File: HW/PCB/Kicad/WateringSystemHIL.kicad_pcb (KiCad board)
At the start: 4 copper layers, 100 x 100 mm, 50 parts, among them J1 USB_B_Micro_VBUS_Input, J13 USB_B_Micro, J16 Boot_H, J17 Boot_L, J18 Encoder_PINA, J19 Encoder_PINB, J20 Encoder_SW, J3 Raspberry Pi Zero WH, J4 MEAS_VIN, J5 MEAS_I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

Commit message: PCB v0.9.1
Added
- Status LEDs for Power, DUT Power, Linked

Changed
- Active signal state of DUT->TS LED and TS->DUT LED. Turn ON the LEDs when the signals are Low level.

Fixed
- An issue where the micro USB plug could not be mounted on the PCB properlly. The micro USB plub was replaced with GCT USB3150.
- An issue where boot mode of WateringSystem was not properlly controlled. Use 74HC244 to control Boot_L signal.
- An issue where power switch of WateringSystem was not properlly controlled. Use a P-Channel MOSFET(AO3401) instead of N-Channel MOSFET(AO3400).
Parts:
- removed J13: USB_B_Micro, WateringSystemHIL:BKL_MicroUSBPlug_10120262
- removed J16: Boot_H, WateringSystemHIL:P100-E2 Pogo Spring Test Probe Pin
- removed Q3: AO3400A, Package_TO_SOT_SMD:SOT-23
- removed R16, R21: 10k, Capacitor_SMD:C_0805_2012Metric_Pad1.18x1.45mm_HandSolder
- added D5: LED_Small, LED_SMD:LED_0603_1608Metric_Pad1.05x0.95mm_HandSolder, F.Cu at (188.4, 131.7)
- added D6: LED_Small, LED_SMD:LED_0603_1608Metric_Pad1.05x0.95mm_HandSolder, F.Cu at (188.4, 133.9)
- added J2: USB_B_Micro, WateringSystemHIL:GCT_USB3150-30-130-A, F.Cu at (149.6, 59.2)
- added R13: 10k, Capacitor_SMD:C_0805_2012Metric_Pad1.18x1.45mm_HandSolder, F.Cu at (184.0, 131.7)
- added R14: 10k, Capacitor_SMD:C_0805_2012Metric_Pad1.18x1.45mm_HandSolder, F.Cu at (184.0, 133.9)
- Q1: value AO3400A -> AO3401A; footprint Package_TO_SOT_SMD:SOT-23 -> Package_TO_SOT_SMD:SOT-23_Handsoldering
- R6: value 10k -> 100
- R8: value 10k -> 10m
- moved R7 7.76 mm to (133.0, 56.2)
- moved R12 3.52 mm to (121.7, 134.6)
- moved D3 2.80 mm to (188.3, 136.2)
- moved R9 2.80 mm to (184.0, 136.2)
- moved D2 1.60 mm to (188.4, 138.4), turned to 180 degrees
- moved R5 1.60 mm to (184.0, 138.4), turned to 0 degrees
- moved D4 0.91 mm to (188.5, 142.8)
- moved R23 0.91 mm to (184.0, 142.8)
- moved Q1 0.82 mm to (133.0, 60.7), turned to 270 degrees
- moved R4 0.30 mm to (184.0, 140.6), turned to 0 degrees
- moved D1 0.28 mm to (188.4, 140.6), turned to 180 degrees
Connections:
- J3 pad 10: Net-(D2-Pad2) -> Net-(D2-Pad1)
- J3 pad 12: CTL_BOOT -> Net-(J3-Pad12)
- J3 pad 40: Net-(J3-Pad40) -> CTL_BOOT
- J3 pad 8: Net-(D1-Pad2) -> Net-(D1-Pad1)
- J7 pad 1: Net-(D1-Pad2) -> Net-(D1-Pad1)
- J8 pad 1: Net-(D2-Pad2) -> Net-(D2-Pad1)
- Q1 pad 2: Net-(Q1-Pad2) -> +5V
- Q1 pad 3: +5V -> Net-(Q1-Pad3)
- R10 pad 2: Net-(Q1-Pad2) -> Net-(Q1-Pad3)
- R4 pad 1: Net-(D1-Pad1) -> +3V3
- R4 pad 2: GND -> Net-(D1-Pad2)
- R5 pad 1: Net-(D2-Pad1) -> +3V3
- R5 pad 2: GND -> Net-(D2-Pad2)
- R7 pad 1: Net-(Q1-Pad1) -> +5V
- R7 pad 2: Net-(Q1-Pad2) -> Net-(Q1-Pad1)
- R8 pad 2: Net-(Q1-Pad2) -> Net-(Q1-Pad3)
- U3 pad 11: Net-(U3-Pad11) -> CTL_BOOT
- U3 pad 2: Net-(U3-Pad2) -> GND
- U3 pad 6: Net-(U3-Pad6) -> GND
- U3 pad 8: Net-(U3-Pad8) -> GND
- U3 pad 9: Net-(U3-Pad9) -> Net-(J17-Pad1)
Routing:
- net +5V: track 44.6 -> 180.3 mm, vias 3 -> 6
- net Net-(D1-Pad1): track 2.49 -> 128.9 mm
- net Net-(D1-Pad2): track 121.5 -> 2.50 mm
- net Net-(D2-Pad1): track 2.49 -> 121.3 mm
- net CTL_POWER: track 17.8 -> 131.0 mm, vias 0 -> 2
- net Net-(D2-Pad2): track 112.5 -> 2.49 mm
- net Net-(J17-Pad1): track 16.5 -> 125.5 mm, vias 0 -> 2
- net Net-(Q1-Pad2): track 39.9 -> 0.00 mm
- net Net-(Q1-Pad3): track 0.00 -> 38.5 mm
- net CTL_BOOT: track 137.5 -> 109.6 mm, vias 2 -> 1
- net GND: track 74.3 -> 100.5 mm, vias 26 -> 37
- net Net-(D3-Pad2): track 101.7 -> 113.9 mm
- net Net-(Q1-Pad1): track 59.6 -> 66.3 mm
- net Net-(Q3-Pad1): track 6.50 -> 0.00 mm
- net Net-(J2-Pad1): track 15.9 -> 22.0 mm, vias 1 -> 0
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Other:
- board text added: "DUT Power"
- board text added: "Power"
- board text added: "Watering system HIL v0.9.1 2021.07.05"
- board text removed: "Watering system HIL v0.9.0 2021.06.23"

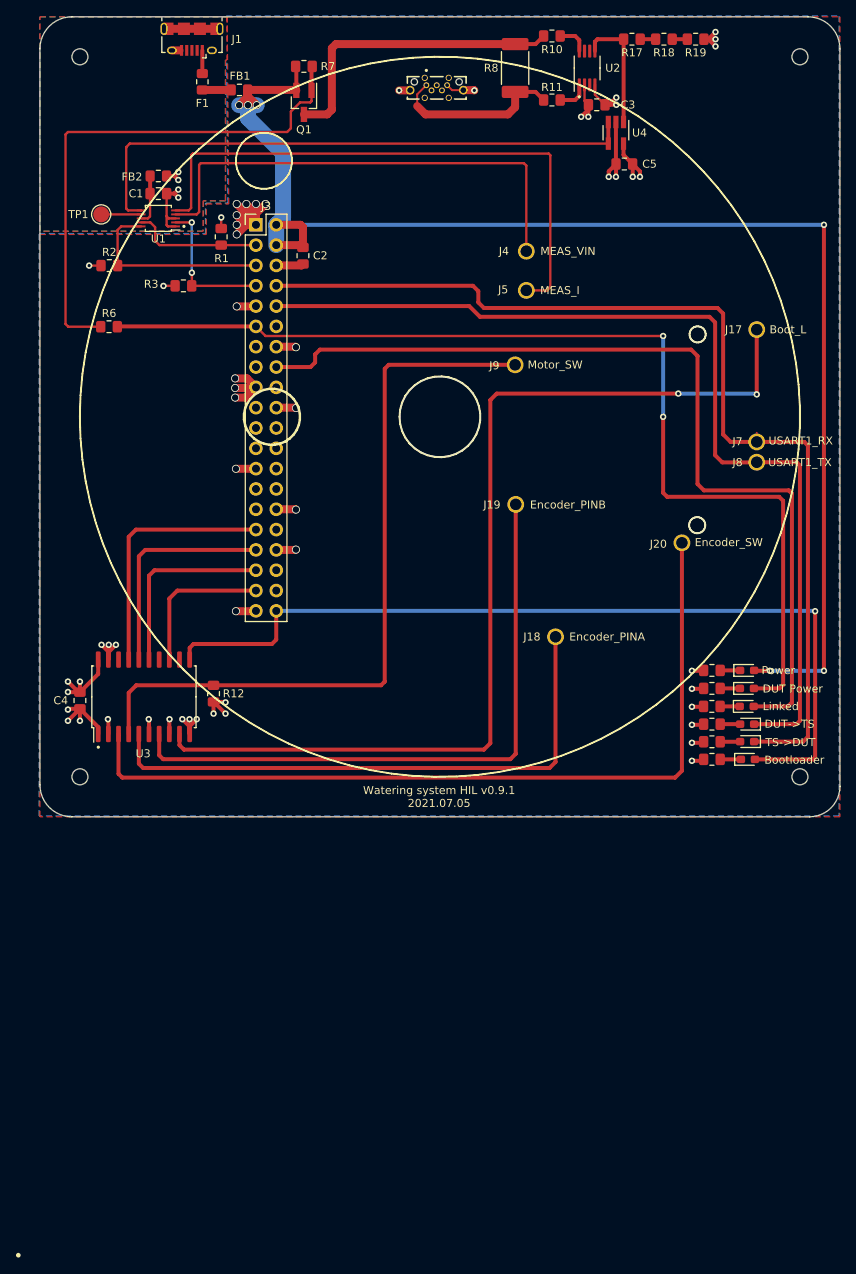
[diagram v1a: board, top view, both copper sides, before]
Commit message: Changed to use a pin socket instead of a pin header for a connector for the Raspberry Pi.
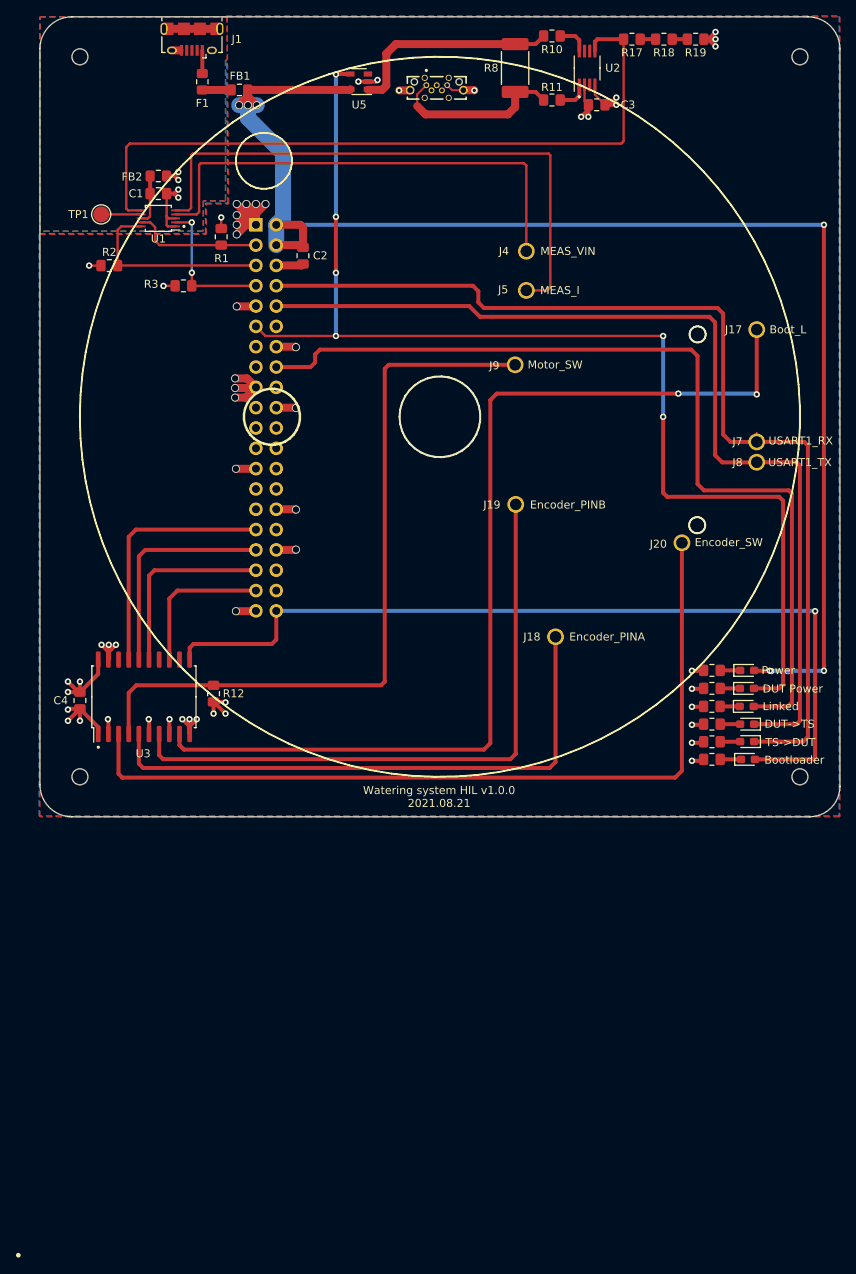
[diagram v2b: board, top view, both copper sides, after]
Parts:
- removed C5: 0.1u, Capacitor_SMD:C_0805_2012Metric_Pad1.18x1.45mm_HandSolder
- removed Q1: AO3401A, Package_TO_SOT_SMD:SOT-23_Handsoldering
- removed R6: 100, Capacitor_SMD:C_0805_2012Metric_Pad1.18x1.45mm_HandSolder
- removed R7: 10k, Capacitor_SMD:C_0805_2012Metric_Pad1.18x1.45mm_HandSolder
- removed U4: LMV321, Package_TO_SOT_SMD:SOT-23-5_HandSoldering
- added U5: AP2151W, Package_TO_SOT_SMD:SOT-23-5, F.Cu at (139.9, 58.1)
- J3: footprint Connector_PinHeader_2.54mm:PinHeader_2x20_P2.54mm_Vertical -> Connector_PinSocket_2.54mm:PinSocket_2x20_P2.54mm_Vertical; moved to B.Cu
- R10: value 10k -> 100
- turned J3 to 180 degrees
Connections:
- J3 pad 31: Encoder_PINA -> Encoder_SW
- J3 pad 35: Encoder_PINB -> Encoder_PINA
- J3 pad 37: Encoder_SW -> Encoder_PINB
- R17 pad 2: Net-(R17-Pad2) -> DUT_CURR
- U2 pad 5: Net-(R17-Pad2) -> DUT_CURR
- U3 pad 13: Encoder_SW -> Encoder_PINB
- U3 pad 15: Encoder_PINB -> Encoder_PINA
- U3 pad 17: Encoder_PINA -> Encoder_SW
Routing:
- net Net-(Q1-Pad1): track 66.3 -> 0.00 mm
- net DUT_CURR: track 72.8 -> 90.3 mm
- net CTL_POWER: track 131.0 -> 148.2 mm, vias 2 -> 6
- net Net-(R17-Pad2): track 15.8 -> 0.00 mm
- net Encoder_SW: track 18.9 -> 31.6 mm
- net Net-(R10-Pad2): track 38.5 -> 27.1 mm
- net Encoder_PINA: track 31.6 -> 24.1 mm
- net +3V3: track 59.1 -> 52.5 mm, vias 24 -> 22
- net GND: track 100.5 -> 94.1 mm
- net Encoder_PINB: track 24.1 -> 18.9 mm
- net +5V: track 180.3 -> 184.0 mm
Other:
- board text added: "Watering system HIL v1.0.0 2021.08.21"
- board text removed: "Watering system HIL v0.9.1 2021.07.05"
